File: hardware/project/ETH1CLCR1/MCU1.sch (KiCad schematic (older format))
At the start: 42 parts, among them J301 Conn_02x01, J302 Conn_02x05, U301 STM32F765ZGT6, U302 24LC08B-E/MS, U303 HDC1080, Y301 NX3225GD-8MHZ-STD-CRA-3

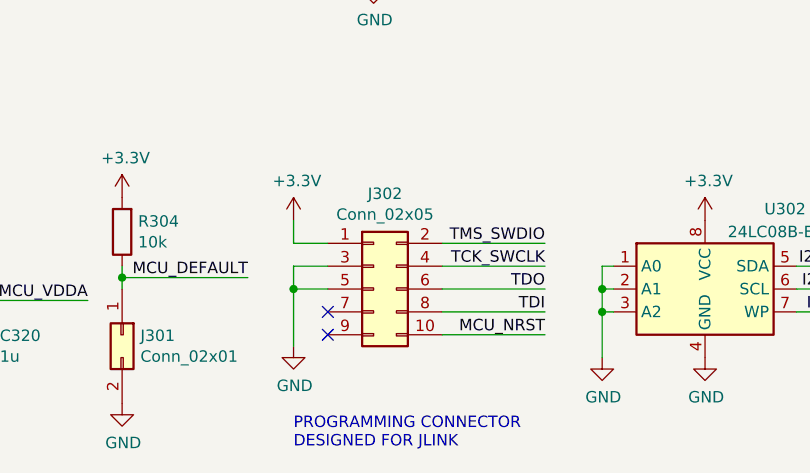
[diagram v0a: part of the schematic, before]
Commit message: Checked the schematics. Created BOM.
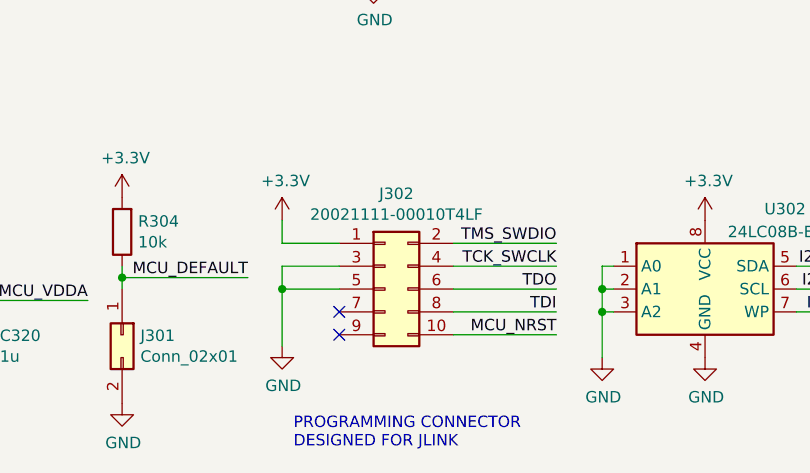
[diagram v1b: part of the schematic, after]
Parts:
- J302: value Conn_02x05 -> 20021111-00010T4LF
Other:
- moved on the sheet: J302
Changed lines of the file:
@@
 L Connector_Generic:Conn_02x05_Odd_Even J302
 U 1 1 5DA8679B
-P 8850 10450
-F 0 "J302" H 8900 10867 50  0000 C CNN
-F 1 "Conn_02x05" H 8900 10776 50  0000 C CNN
-F 2 "Connector_PinHeader_1.27mm:PinHeader_2x05_P1.27mm_Vertical" H 8850 10450 50  0001 C CNN
-F 3 "~" H 8850 10450 50  0001 C CNN
-	1    8850 10450
+P 8900 10450
+F 0 "J302" H 8950 10867 50  0000 C CNN
+F 1 "20021111-00010T4LF" H 8950 10776 50  0000 C CNN
+F 2 "Connector_PinHeader_1.27mm:PinHeader_2x05_P1.27mm_Vertical" H 8900 10450 50  0001 C CNN
+F 3 "~" H 8900 10450 50  0001 C CNN
+	1    8900 10450
 	1    0    0    -1
 $EndComp
-NoConn ~ 8650 10550
-NoConn ~ 8650 10650
+NoConn ~ 8700 10550
+NoConn ~ 8700 10650
 Wire Wire Line
-	8650 10450 8500 10450
+	8700 10450 8450 10450
 Wire Wire Line
-	8500 10450 8500 10350
+	8450 10450 8450 10350
 Wire Wire Line
-	8500 10350 8650 10350
+	8450 10350 8700 10350
 $Comp
 L power:GND #PWR0315
 U 1 1 5DAA5490
-P 8500 10700
-F 0 "#PWR0315" H 8500 10450 50  0001 C CNN
-F 1 "GND" H 8505 10527 50  0000 C CNN
-F 2 "" H 8500 10700 50  0001 C CNN
-F 3 "" H 8500 10700 50  0001 C CNN
-	1    8500 10700
+P 8450 10700
+F 0 "#PWR0315" H 8450 10450 50  0001 C CNN
+F 1 "GND" H 8455 10527 50  0000 C CNN
+F 2 "" H 8450 10700 50  0001 C CNN
+F 3 "" H 8450 10700 50  0001 C CNN
+	1    8450 10700
 	1    0    0    -1
 $EndComp
 Wire Wire Line
-	8500 10700 8500 10450
-Connection ~ 8500 10450
+	8450 10700 8450 10450
+Connection ~ 8450 10450
 $Comp
 L power:+3.3V #PWR0314
 U 1 1 5DAA706A
-P 8500 10150
-F 0 "#PWR0314" H 8500 10000 50  0001 C CNN
-F 1 "+3.3V" H 8515 10323 50  0000 C CNN
-F 2 "" H 8500 10150 50  0001 C CNN
-F 3 "" H 8500 10150 50  0001 C CNN
-	1    8500 10150
+P 8450 10150
+F 0 "#PWR0314" H 8450 10000 50  0001 C CNN
+F 1 "+3.3V" H 8465 10323 50  0000 C CNN
+F 2 "" H 8450 10150 50  0001 C CNN
+F 3 "" H 8450 10150 50  0001 C CNN
+	1    8450 10150
 	1    0    0    -1
 $EndComp
 Wire Wire Line
-	8500 10150 8500 10250
+	8450 10150 8450 10250
 Wire Wire Line
-	8500 10250 8650 10250
+	8450 10250 8700 10250
 Wire Wire Line
-	9150 10250 9600 10250
-Text Label 9600 10250 2    50   ~ 0
+	9200 10250 9650 10250
+Text Label 9650 10250 2    50   ~ 0
 TMS_SWDIO
 Wire Wire Line
-	9150 10350 9600 10350
-Text Label 9600 10350 2    50   ~ 0
+	9200 10350 9650 10350
+Text Label 9650 10350 2    50   ~ 0
 TCK_SWCLK
 Wire Wire Line
-	9150 10450 9600 10450
-Text Label 9600 10450 2    50   ~ 0
+	9200 10450 9650 10450
+Text Label 9650 10450 2    50   ~ 0
 TDO
 Wire Wire Line
-	9150 10550 9600 10550
-Text Label 9600 10550 2    50   ~ 0
+	9200 10550 9650 10550
+Text Label 9650 10550 2    50   ~ 0
 TDI
 Wire Wire Line
-	9150 10650 9600 10650
-Text Label 9600 10650 2    50   ~ 0
+	9200 10650 9650 10650
+Text Label 9650 10650 2    50   ~ 0
 MCU_NRST
 Text Label 15650 8300 2    50   ~ 0

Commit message: PCB layout
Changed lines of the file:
@@
 L power:GND #PWR0103
 U 1 1 5EFC3E57
-P 1100 10000
-F 0 "#PWR0103" H 1100 9750 50  0001 C CNN
-F 1 "GND" H 1105 9827 50  0000 C CNN
-F 2 "" H 1100 10000 50  0001 C CNN
-F 3 "" H 1100 10000 50  0001 C CNN
-	1    1100 10000
+P 1100 10100
+F 0 "#PWR0103" H 1100 9850 50  0001 C CNN
+F 1 "GND" H 1105 9927 50  0000 C CNN
+F 2 "" H 1100 10100 50  0001 C CNN
+F 3 "" H 1100 10100 50  0001 C CNN
+	1    1100 10100
 	1    0    0    -1
 $EndComp
@@
 Text Label 2700 1500 0    50   ~ 0
 SENS_SDA
+Wire Wire Line
+	1100 10100 1100 10000
 $EndSCHEMATC

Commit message: PCB layout
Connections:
- net MCU1_GPIO_OUT1: now also U301.63 (PE10,TIM1_CH2N,DFSDM1_DATIN4,UART7_CTS,QUADSPI_BK2_IO3,FMC_D7,EVENTOUT); no longer U301.22 (PF10,QUADSPI_CLK,DCMI_D11,LCD_DE,EVENTOUT,ADC3_IN8)
- net MCU1_GPIO_OUT2: now also U301.60 (PE9,TIM1_CH1,DFSDM1_CKOUT,UART7_RTS,QUADSPI_BK2_IO2,FMC_D6,EVENTOUT); no longer U301.26 (PC0,DFSDM1_CKIN0,DFSDM1_DATIN4,SAI2_FS_B,OTG_HS_ULPI_STP,FMC_SDNWE,LCD_R5,EVENTOUT,ADC1_IN10,ADC2_IN10,ADC3_IN10)
- net MCU1_MCLK: now also U301.65 (PE12,TIM1_CH3N,SPI4_SCK,DFSDM1_DATIN5,SAI2_SCK_B,FMC_D9,LCD_B4,EVENTOUT); no longer U301.19 (PF7,TIM11_CH1,SPI5_SCK,SAI1_MCLK_B,UART7_TX,QUADSPI_BK1_IO2,EVENTOUT,ADC3_IN5)
- net MCU1_MISO: now also U301.66 (PE13,TIM1_CH3,SPI4_MISO,DFSDM1_CKIN5,SAI2_FS_B,FMC_D10,LCD_DE,EVENTOUT); no longer U301.20 (PF8,SPI5_MISO,SAI1_SCK_B,UART7_RTS,TIM13_CH1,QUADSPI_BK1_IO0,EVENTOUT,ADC3_IN6)
- net MCU1_MOSI: now also U301.67 (PE14,TIM1_CH4,SPI4_MOSI,SAI2_MCLK_B,FMC_D11,LCD_CLK,EVENTOUT); no longer U301.21 (PF9,SPI5_MOSI,SAI1_FS_B,UART7_CTS,TIM14_CH1,QUADSPI_BK1_IO1,EVENTOUT,ADC3_IN7)
- net MCU1_~SS: now also U301.64 (PE11,TIM1_CH2,SPI4_NSS,DFSDM1_CKIN4,SAI2_SD_B,FMC_D8,LCD_G3,EVENTOUT); no longer U301.18 (PF6,TIM10_CH1,SPI5_NSS,SAI1_SD_B,UART7_RX,QUADSPI_BK1_IO3,EVENTOUT,ADC3_IN4)
- net TRIG_EN: now also U301.3 (PE4,TRACED1,SPI4_NSS,SAI1_FS_A,DFSDM1_DATIN3,FMC_A20,DCMI_D4,LCD_B0,EVENTOUT); no longer U301.74 (PB13,TIM1_CH1N,SPI2_SCK,I2S2_CK,DFSDM1_CKIN1,USART3_CTS,UART5_TX,CAN2_TX,OTG_HS_ULPI_D6,ETH_MII_TXD1,ETH_RMII_TXD1,EVENTOUT,OTG_HS_VBUS)
- net TRIG_IN: now also U301.1 (PE2,TRACECLK,SPI4_SCK,SAI1_MCLK_A,QUADSPI_BK1_IO2,ETH_MII_TXD3,FMC_A23,EVENTOUT); no longer U301.76 (PB15,RTC_REFIN,TIM1_CH3N,TIM8_CH3N,USART1_RX,SPI2_MOSI,I2S2_SD,DFSDM1_CKIN2,UART4_CTS,TIM12_CH2,SDMMC2_D1,OTG_HS_DP,EVENTOUT)
- net TRIG_OUT: now also U301.2 (PE3,TRACED0,SAI1_SD_B,FMC_A19,EVENTOUT); no longer U301.75 (PB14,TIM1_CH2N,TIM8_CH2N,USART1_TX,SPI2_MISO,DFSDM1_DATIN2,USART3_RTS,UART4_RTS,TIM12_CH1,SDMMC2_D0,OTG_HS_DM,EVENTOUT)
- net MCU1_STATUS_IN2: now reaches U301.58 (PE7,TIM1_ETR,DFSDM1_DATIN2,UART7_RX,QUADSPI_BK2_IO0,FMC_D4,EVENTOUT)
- net MCU1_STATUS_IN1: now reaches U301.59 (PE8,TIM1_CH1N,DFSDM1_CKIN2,UART7_TX,QUADSPI_BK2_IO1,FMC_D5,EVENTOUT)
- net MCU1_STATUS_IN: no longer names the net of U301.28 (PC2,DFSDM1_CKIN1,SPI2_MISO,DFSDM1_CKOUT,OTG_HS_ULPI_DIR,ETH_MII_TXD2,FMC_SDNE0,EVENTOUT,ADC1_IN12,ADC2_IN12,ADC3_IN12)
- no-connect marks 82 -> 81
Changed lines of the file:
@@
 Wire Wire Line
 	650  9700 650  9600
-Text HLabel 14600 7600 2    50   Output ~ 0
+Text HLabel 14600 5000 2    50   Output ~ 0
 TRIG_EN
-Text HLabel 14600 7700 2    50   Output ~ 0
+Text HLabel 14600 4900 2    50   Output ~ 0
 TRIG_OUT
-Text HLabel 14600 7800 2    50   Input ~ 0
+Text HLabel 14600 4800 2    50   Input ~ 0
 TRIG_IN
 Wire Wire Line
 	14550 8300 15200 8300
 Wire Wire Line
-	14600 7600 14550 7600
-Wire Wire Line
-	14600 7700 14550 7700
-Wire Wire Line
-	14550 7800 14600 7800
-Text HLabel 3100 5100 0    50   Input ~ 0
-MCU1_STATUS_IN
-Text HLabel 3100 4900 0    50   Output ~ 0
+	14600 4800 14550 4800
+Wire Wire Line
+	14600 4900 14550 4900
+Wire Wire Line
+	14550 5000 14600 5000
+Text HLabel 14600 5400 2    50   Input ~ 0
+MCU1_STATUS_IN1
+Text HLabel 14600 5500 2    50   Output ~ 0
 MCU1_GPIO_OUT2
-Text HLabel 3100 2500 0    50   Output ~ 0
+Text HLabel 14600 5600 2    50   Output ~ 0
 MCU1_GPIO_OUT1
 Wire Wire Line
-	3100 2500 3150 2500
-Wire Wire Line
-	3150 4900 3100 4900
-Wire Wire Line
-	3100 5100 3150 5100
-Wire Wire Line
-	3150 2100 3100 2100
-Wire Wire Line
-	3100 2200 3150 2200
-Wire Wire Line
-	3150 2300 3100 2300
-Wire Wire Line
-	3100 2400 3150 2400
-Text HLabel 3100 2100 0    50   Output ~ 0
+	14600 5500 14550 5500
+Wire Wire Line
+	14550 5600 14600 5600
+Wire Wire Line
+	14600 5400 14550 5400
+Wire Wire Line
+	14550 5700 14600 5700
+Wire Wire Line
+	14600 5800 14550 5800
+Wire Wire Line
+	14550 5900 14600 5900
+Wire Wire Line
+	14600 6000 14550 6000
+Text HLabel 14600 5700 2    50   Output ~ 0
 MCU1_~SS
-Text HLabel 3100 2300 0    50   Input ~ 0
+Text HLabel 14600 5900 2    50   Input ~ 0
 MCU1_MISO
-Text HLabel 3100 2400 0    50   Output ~ 0
+Text HLabel 14600 6000 2    50   Output ~ 0
 MCU1_MOSI
-Text HLabel 3100 2200 0    50   Output ~ 0
+Text HLabel 14600 5800 2    50   Output ~ 0
 MCU1_MCLK
 Wire Wire Line
@@
 NoConn ~ 14550 4600
 NoConn ~ 14550 4700
-NoConn ~ 14550 4800
-NoConn ~ 14550 4900
-NoConn ~ 14550 5000
 NoConn ~ 14550 5100
 NoConn ~ 14550 5200
-NoConn ~ 14550 5300
-NoConn ~ 14550 5400
-NoConn ~ 14550 5500
-NoConn ~ 14550 5600
-NoConn ~ 14550 5700
-NoConn ~ 14550 5800
-NoConn ~ 14550 5900
-NoConn ~ 14550 6000
 NoConn ~ 14550 6100
 NoConn ~ 14550 6300
@@
 Wire Wire Line
 	1100 10100 1100 10000
+NoConn ~ 3150 2100
+NoConn ~ 3150 2200
+NoConn ~ 3150 2300
+NoConn ~ 3150 2400
+NoConn ~ 3150 2500
+NoConn ~ 3150 4900
+NoConn ~ 3150 5100
+Text HLabel 14600 5300 2    50   Input ~ 0
+MCU1_STATUS_IN2
+Wire Wire Line
+	14600 5300 14550 5300
+NoConn ~ 14550 7600
+NoConn ~ 14550 7700
+NoConn ~ 14550 7800
 $EndSCHEMATC

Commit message: PCB layout
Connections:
- net MCU_DEFAULT: now also U301.119 (PD5,USART2_TX,FMC_NWE,EVENTOUT); no longer U301.104 (PA12,TIM1_ETR,SPI2_SCK,I2S2_CK,UART4_TX,USART1_RTS,SAI2_FS_B,CAN1_TX,OTG_FS_DP,LCD_R5,EVENTOUT)
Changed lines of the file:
@@
 NoConn ~ 14550 3200
 NoConn ~ 14550 3300
-NoConn ~ 14550 3400
 NoConn ~ 14550 3500
 NoConn ~ 14550 3600
@@
 	3650 10900 4150 10900
 Wire Wire Line
-	3150 4400 2600 4400
-Text Label 2600 4400 0    50   ~ 0
+	14550 3400 15100 3400
+Text Label 15100 3400 2    50   ~ 0
 MCU_DEFAULT
 Connection ~ 11400 9950
@@
 NoConn ~ 14550 7700
 NoConn ~ 14550 7800
+NoConn ~ 3150 4400
 $EndSCHEMATC
